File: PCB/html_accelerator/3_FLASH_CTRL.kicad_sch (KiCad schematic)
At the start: 2 parts, among them U2 AU6438BS, U3 MX30LF1G28AD-TI

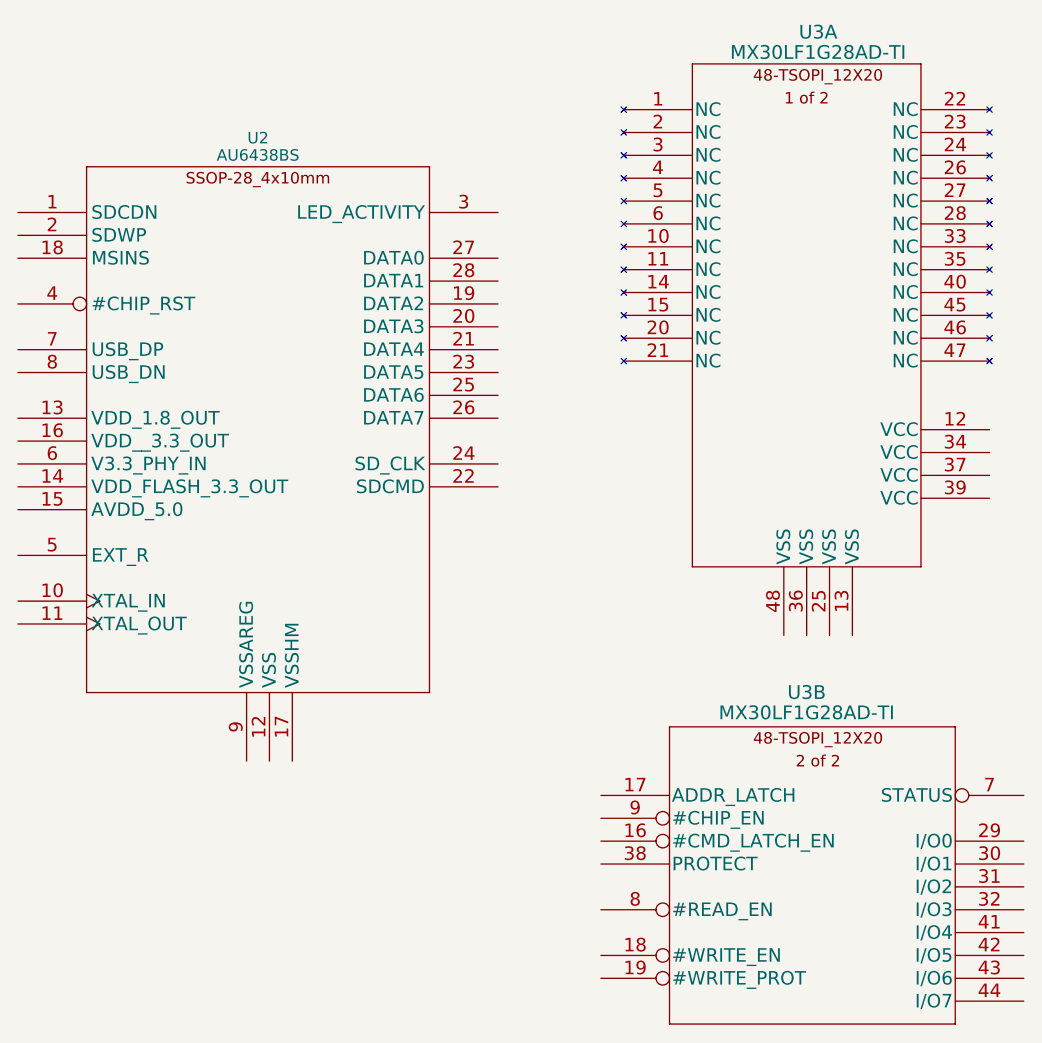
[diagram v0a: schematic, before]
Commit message: Update to MCS9990 for PCIE direct to USB
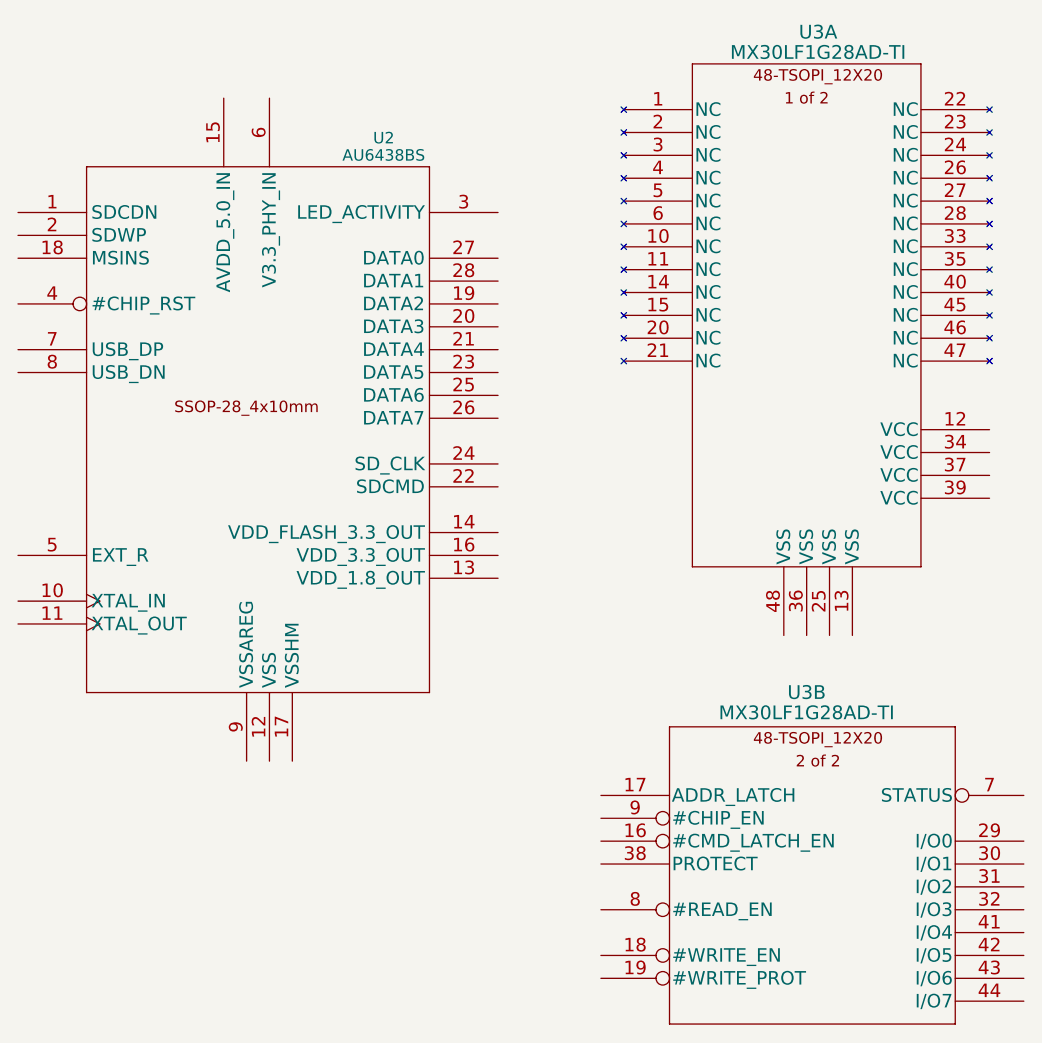
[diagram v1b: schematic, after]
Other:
- moved on the sheet: U2
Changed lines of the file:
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@@
   (symbol (lib_id "html_accel_Symbols:AU6438BS") (at 46.99 44.45 0) (unit 1)
     (in_bom yes) (on_board yes) (dnp no)
-    (property "Reference" "U2" (at 66.04 41.259 0)
+    (property "Reference" "U2" (at 80.01 41.259 0)
       (effects (font (size 1.27 1.27)))
     )
-    (property "Value" "AU6438BS" (at 66.04 43.18 0)
+    (property "Value" "AU6438BS" (at 80.01 43.18 0)
       (effects (font (size 1.27 1.27)))
     )
